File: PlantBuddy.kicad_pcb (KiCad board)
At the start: 4 copper layers, 44.3 x 29.2 mm, 47 parts, among them J1 USB_C_Receptacle_USB2.0, J101 JST, J4 External, SW1 SW_Push, U1 LTR-303ALS-01, U101 TPS2051B, U102 ESP32-S3-MINI-1-N8, U103 TPS2051B, U2 SHTC3, U4 BQ24072RGT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

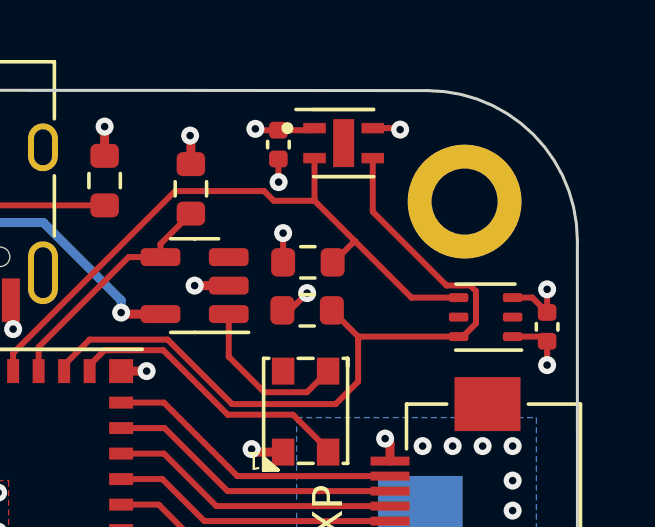
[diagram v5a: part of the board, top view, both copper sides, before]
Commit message: Added copper heatsink to temperature sensor.
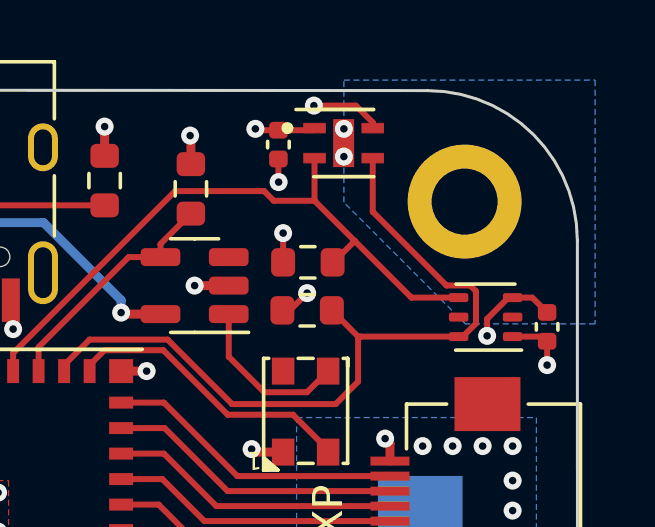
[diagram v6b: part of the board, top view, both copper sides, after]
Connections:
- H104 pad 1: GND -> unconnected-(U2-Pad5)
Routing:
- net GND: track 62.3 -> 64.7 mm
- net unconnected-(U2-Pad5): vias 0 -> 2
- added copper zone on B.Cu, net unconnected-(U2-Pad5)
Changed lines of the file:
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@@
     (fp_circle (center 0 0) (end 2.15 0) (layer "F.CrtYd") (width 0.05) (fill none))
     (pad "1" thru_hole circle locked (at 0 0) (size 3.8 3.8) (drill 2.2) (layers *.Cu *.Mask)
-      (net 6 "GND") (thermal_width 2))
+      (net 21 "unconnected-(U2-Pad5)") (thermal_width 2))
   )
   (footprint "Connector_Molex:Molex_PicoBlade_53261-0271_1x02-1MP_P1.25mm_Horizontal" (layer "F.Cu")
@@
   (segment (start 151.67533 131.381171) (end 150.51283 131.381171) (width 0.3) (layer "F.Cu") (net 6))
   (segment (start 126.01908 122.631171) (end 126.01908 121.731171) (width 0.2) (layer "F.Cu") (net 6))
+  (segment (start 152.74458 113.331171) (end 151.34408 113.331171) (width 0.2) (layer "F.Cu") (net 6))
   (segment (start 150.41908 133.681171) (end 150.36908 133.631171) (width 0.3) (layer "F.Cu") (net 6))
   (segment (start 147.29408 139.356027) (end 147.29408 138.456171) (width 0.2) (layer "F.Cu") (net 6))
+  (segment (start 153.30658 113.893171) (end 152.74458 113.331171) (width 0.2) (layer "F.Cu") (net 6))
   (segment (start 126.31908 127.256171) (end 126.29408 127.281171) (width 0.2) (layer "F.Cu") (net 6))
   (segment (start 125.57308 128.689671) (end 125.57308 127.967221) (width 0.2) (layer "F.Cu") (net 6))
@@
   (segment (start 141.24408 120.706171) (end 141.31908 120.781171) (width 0.3) (layer "F.Cu") (net 6))
   (segment (start 146.46908 136.461171) (end 146.46908 137.281171) (width 0.2) (layer "F.Cu") (net 6))
+  (segment (start 153.30658 114.081171) (end 153.30658 113.893171) (width 0.2) (layer "F.Cu") (net 6))
   (segment (start 150.51283 131.381171) (end 150.46283 131.431171) (width 0.3) (layer "F.Cu") (net 6))
   (segment (start 146.46908 134.511171) (end 146.84908 134.131171) (width 0.3) (layer "F.Cu") (net 6))
@@
   (segment (start 123.24408 122.756171) (end 123.26908 122.731171) (width 0.3) (layer "F.Cu") (net 6))
   (segment (start 148.04408 137.131171) (end 148.04408 138.056171) (width 0.2) (layer "F.Cu") (net 6))
+  (segment (start 157.96908 119.731171) (end 157.828804 119.731171) (width 0.2) (layer "F.Cu") (net 6))
   (segment (start 130.91908 133.431171) (end 130.91908 132.581171) (width 0.3) (layer "F.Cu") (net 6))
+  (segment (start 157.828804 119.731171) (end 157.11908 120.440895) (width 0.2) (layer "F.Cu") (net 6))
   (segment (start 153.881499 125.181171) (end 153.881499 124.59359) (width 0.3) (layer "F.Cu") (net 6))
   (segment (start 147.86283 130.776171) (end 147.08908 130.776171) (width 0.3) (layer "F.Cu") (net 6))
@@
   (segment (start 144.91908 135.131171) (end 144.91908 134.281171) (width 0.3) (layer "F.Cu") (net 6))
   (segment (start 130.91908 136.181171) (end 144.91908 136.181171) (width 0.3) (layer "F.Cu") (net 6))
-  (segment (start 154.16908 114.081171) (end 154.21908 114.131171) (width 0.2) (layer "F.Cu") (net 6))
+  (segment (start 157.11908 120.440895) (end 157.11908 121.006171) (width 0.2) (layer "F.Cu") (net 6))
   (segment (start 139.56908 130.831171) (end 139.56908 129.181171) (width 0.3) (layer "F.Cu") (net 6))
   (segment (start 127.59408 121.856171) (end 127.56908 121.831171) (width 0.2) (layer "F.Cu") (net 6))
@@
   (segment (start 125.56908 128.693671) (end 125.45658 128.693671) (width 0.3) (layer "F.Cu") (net 6))
   (segment (start 123.24408 128.906171) (end 123.51908 129.181171) (width 0.3) (layer "F.Cu") (net 6))
-  (segment (start 159.11908 120.226171) (end 159.11908 119.456171) (width 0.2) (layer "F.Cu") (net 6))
   (segment (start 126.06908 125.818671) (end 126.06908 125.134671) (width 0.2) (layer "F.Cu") (net 6))
   (segment (start 148.50658 119.331171) (end 147.36908 119.331171) (width 0.3) (layer "F.Cu") (net 6))
@@
   (segment (start 134.74408 119.816171) (end 134.74408 120.256171) (width 0.3) (layer "F.Cu") (net 6))
   (segment (start 123.14408 130.256171) (end 123.14408 130.956171) (width 0.3) (layer "F.Cu") (net 6))
-  (segment (start 153.30658 114.081171) (end 154.16908 114.081171) (width 0.2) (layer "F.Cu") (net 6))
   (segment (start 127.75658 117.331171) (end 128.99408 117.331171) (width 0.3) (layer "F.Cu") (net 6))
   (segment (start 125.44408 133.406171) (end 125.44408 134.456171) (width 0.3) (layer "F.Cu") (net 6))
@@
   (via (at 154.96908 124.681171) (size 0.6) (drill 0.25) (layers "F.Cu" "B.Cu") (free) (net 6))
   (via (at 135.06908 131.931171) (size 0.6) (drill 0.25) (layers "F.Cu" "B.Cu") (free) (net 6))
-  (via (at 159.11908 119.456171) (size 0.6) (drill 0.25) (layers "F.Cu" "B.Cu") (net 6))
   (via (at 135.06908 127.531171) (size 0.6) (drill 0.25) (layers "F.Cu" "B.Cu") (free) (net 6))
   (via (at 139.56908 126.231171) (size 0.6) (drill 0.25) (layers "F.Cu" "B.Cu") (free) (net 6))
@@
   (via (at 153.71908 124.431171) (size 0.6) (drill 0.25) (layers "F.Cu" "B.Cu") (net 6))
   (via (at 140.81908 129.181171) (size 0.6) (drill 0.25) (layers "F.Cu" "B.Cu") (free) (net 6))
-  (via (at 154.21908 114.131171) (size 0.6) (drill 0.25) (layers "F.Cu" "B.Cu") (net 6))
   (via (at 123.26908 122.731171) (size 0.6) (drill 0.25) (layers "F.Cu" "B.Cu") (net 6))
   (via (at 123.51908 129.181171) (size 0.6) (drill 0.25) (layers "F.Cu" "B.Cu") (net 6))
@@
   (via (at 136.21908 135.131171) (size 0.6) (drill 0.25) (layers "F.Cu" "B.Cu") (free) (net 6))
   (via (at 134.11908 120.881171) (size 0.6) (drill 0.25) (layers "F.Cu" "B.Cu") (net 6))
+  (via (at 151.34408 113.331171) (size 0.6) (drill 0.25) (layers "F.Cu" "B.Cu") (net 6))
   (via (at 137.91908 135.131171) (size 0.6) (drill 0.25) (layers "F.Cu" "B.Cu") (free) (net 6))
   (via (at 156.96908 124.681171) (size 0.6) (drill 0.25) (layers "F.Cu" "B.Cu") (free) (net 6))
@@
   (via (at 150.36908 133.631171) (size 0.6) (drill 0.25) (layers "F.Cu" "B.Cu") (net 6))
   (via (at 148.01908 138.081171) (size 0.6) (drill 0.25) (layers "F.Cu" "B.Cu") (net 6))
+  (via (at 157.11908 121.006171) (size 0.6) (drill 0.25) (layers "F.Cu" "B.Cu") (net 6))
   (via (at 137.91908 126.231171) (size 0.6) (drill 0.25) (layers "F.Cu" "B.Cu") (free) (net 6))
   (via (at 129.21908 121.831171) (size 0.6) (drill 0.25) (layers "F.Cu" "B.Cu") (net 6))
@@
   (segment (start 144.61908 131.731171) (end 144.06908 131.731171) (width 0.2) (layer "B.Cu") (net 19))
   (segment (start 132.01908 132.581171) (end 129.71908 132.581171) (width 0.2) (layer "B.Cu") (net 19))
+  (via (at 152.34408 115.031171) (size 0.6) (drill 0.25) (layers "F.Cu" "B.Cu") (net 21))
+  (via (at 152.34408 114.106171) (size 0.6) (drill 0.25) (layers "F.Cu" "B.Cu") (net 21))
   (segment (start 137.24408 119.816171) (end 137.24408 118.862571) (width 0.2286) (layer "F.Cu") (net 22))
   (segment (start 138.01238 118.824471) (end 138.24408 119.056171) (width 0.2286) (layer "F.Cu") (net 22))
@@
     )
   )
+  (zone (net 21) (net_name "unconnected-(U2-Pad5)") (layer "B.Cu") (hatch edge 0.508)
+    (connect_pads (clearance 0))
+    (min_thickness 0.254) (filled_areas_thickness no)
+    (fill yes (thermal_gap 0.508) (thermal_bridge_width 0.508))
+    (polygon
+      (pts
+        (xy 160.71908 120.606171)
+        (xy 156.39408 120.606171)
+        (xy 152.34408 116.556171)
+        (xy 152.34408 112.481171)
+        (xy 160.71908 112.481171)
+      )
+    )
+  )
   (zone (net 6) (net_name "GND") (layer "B.Cu") (hatch edge 0.508)
     (connect_pads (clearance 0))
@@
       )
     )
+  )
+  (zone (net 0) (net_name "") (layer "B.Mask") (hatch edge 0.508)
+    (connect_pads (clearance 0))
+    (min_thickness 0.254) (filled_areas_thickness no)
+    (fill yes (thermal_gap 0.508) (thermal_bridge_width 0.508))
+    (polygon
+      (pts
+        (xy 160.71908 120.606171)
+        (xy 156.39408 120.606171)
+        (xy 152.34408 116.556171)
+        (xy 152.34408 112.481171)
+        (xy 160.71908 112.481171)
+      )
+    )

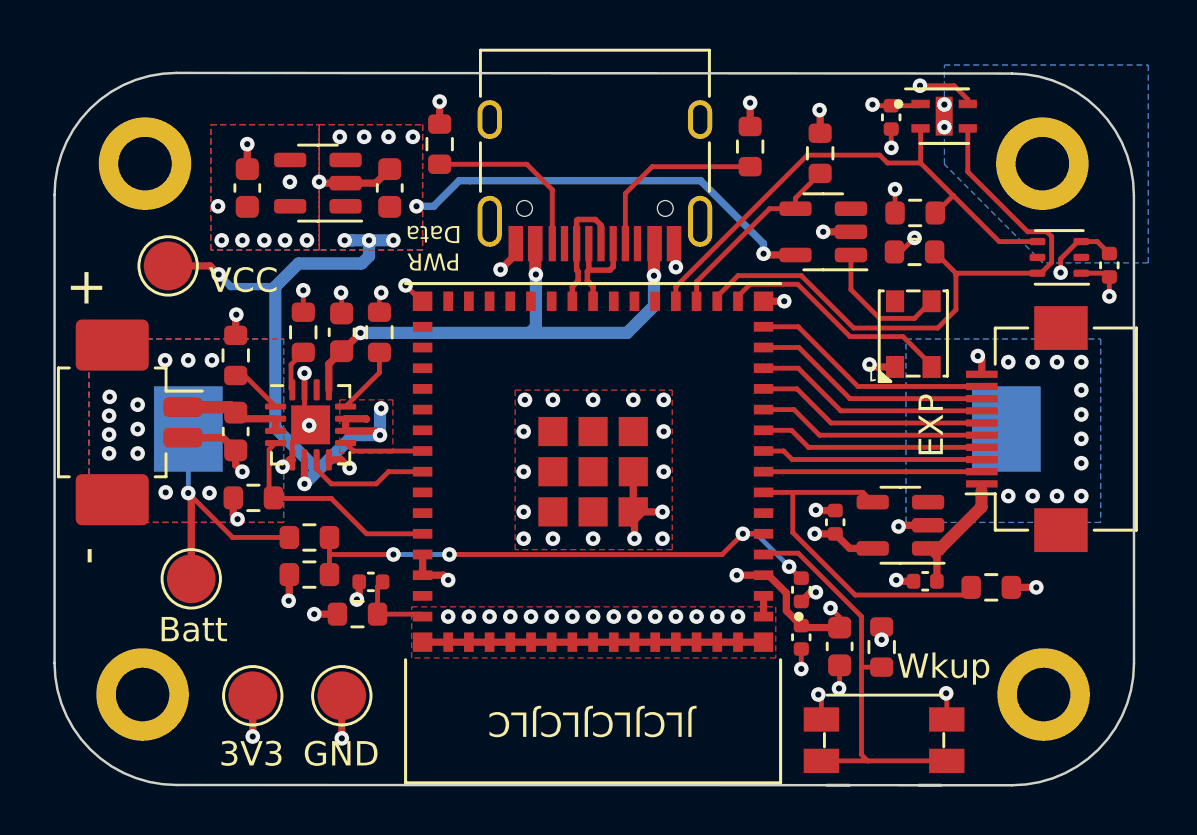
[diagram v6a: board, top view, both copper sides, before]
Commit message: Multitude of changes. Hopefully design freeze.
- Switched JST connector to a bigger 2mm pitch one.
- Added battery protection circuit for coin cell.
- Created cutout in PCB for battery cable.
- Added heatsink for SHTC3.
- Added plated mounting holes for looks and power dissipation.
- Changed pin layout to facilitate wake-up via USB-C plug-in detection.
- Added ARTech logo.
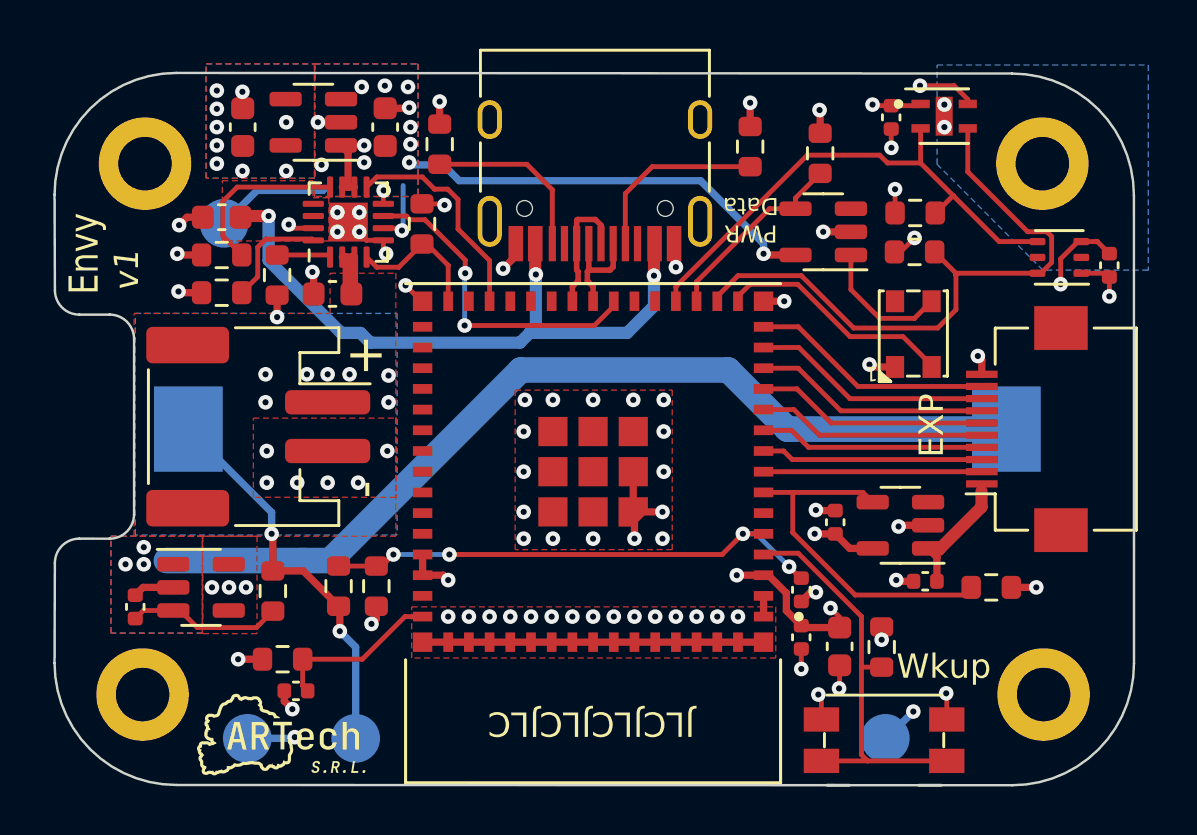
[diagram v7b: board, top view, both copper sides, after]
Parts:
- added C104: 100nF, Capacitor_SMD:C_0402_1005Metric, F.Cu at (119.1, 134.7)
- added G***: LOGO, LOGO, F.Cu at (125.2, 139.9)
- added R103: 100R, Resistor_SMD:R_0603_1608Metric, F.Cu at (124.8, 134.1)
- added U104: XB5350A, Package_TO_SOT_SMD:SOT-23-5, F.Cu at (121.8, 133.9)
- J101: footprint Connector_Molex:Molex_PicoBlade_53261-0271_1x02-1MP_P1.25mm_Horizontal -> Connector_JST:JST_PH_S2B-PH-SM4-TB_1x02-1MP_P2.00mm_Horizontal
- R6: value 15k -> 9.1k
- R8, R9: value 15k -> 10k
- TP1, TP101, TP102, TP2: moved to B.Cu
- moved TP1 26.0 mm to (149.9, 140.1), turned to 180 degrees
- moved R9 13.2 mm to (130.9, 119.0), turned to -90 degrees
- moved TP102 9.41 mm to (128.2, 140.1), turned to 180 degrees
- moved U4 8.47 mm to (127.9, 118.9), turned to 90 degrees
- moved R5 7.21 mm to (122.7, 120.3), turned to 0 degrees
- moved C6 6.91 mm to (127.2, 121.9), turned to 0 degrees
- moved C5 6.83 mm to (122.7, 118.7), turned to 180 degrees
- moved J101 5.50 mm to (124.2, 127.3)
- moved C3 5.43 mm to (125.7, 138.2)
- moved TP2 4.26 mm to (123.7, 140.1), turned to 180 degrees
- moved R6 3.72 mm to (122.7, 121.8), turned to 0 degrees
- moved R10 3.71 mm to (124.9, 121.1), turned to -90 degrees
- moved R8 3.59 mm to (125.2, 136.9)
- moved TP101 2.89 mm to (122.8, 119.0), turned to 180 degrees
- moved R14 2.79 mm to (129.0, 133.9), turned to -90 degrees
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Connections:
- BT1 pad 2: GND -> /Bat_n
- H104 pad 1: unconnected-(U2-Pad5) -> /Heat
- U102 pad 22: unconnected-(U102-Pad22) -> /~PGOOD
- U102 pad 28: unconnected-(U102-Pad28) -> /~CHG
- U102 pad 30: unconnected-(U102-Pad30) -> /charge_disable
- U102 pad 37: /~CHG -> unconnected-(U102-Pad37)
- U102 pad 38: /~PGOOD -> unconnected-(U102-Pad38)
- U102 pad 41: /charge_disable -> unconnected-(U102-Pad41)
- U2 pad 5: unconnected-(U2-Pad5) -> /Heat
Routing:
- net /Bat_n: track 0.00 -> 40.7 mm, vias 0 -> 3
- net VCC: track 46.4 -> 27.4 mm, vias 13 -> 11
- net /~PGOOD: track 5.19 -> 13.5 mm, vias 0 -> 2
- net Net-(C104-Pad1): track 0.00 -> 6.36 mm
- net +BATT: track 15.6 -> 21.5 mm, vias 13 -> 9
- net /~CHG: track 3.30 -> 9.03 mm
- net VBUS: track 21.8 -> 27.2 mm
- net Net-(R5-Pad2): track 2.80 -> 7.16 mm
- net GND: track 64.7 -> 60.4 mm, vias 79 -> 80
- net /~{tRST}: track 3.30 -> 7.03 mm
- net /charge_disable: track 9.17 -> 5.76 mm
- net Net-(R6-Pad2): track 1.77 -> 4.58 mm
- net /batsense: track 22.9 -> 21.2 mm
- net +3V3: vias 19 -> 20
- net unconnected-(U2-Pad5): vias 2 -> 0
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- added copper zone on B.Cu, net /Bat_n
- added copper zone on F.Cu, net /Bat_n
- added copper zone on B.Cu, net /Heat
- added copper zone on F.Cu, net VBUS
- removed copper zone on B.Cu, net GND
- removed copper zone on B.Cu, net unconnected-(U2-Pad5)
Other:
- outline, holes or cut-outs redrawn
- board text added: "Envy"
- board text added: "v1"

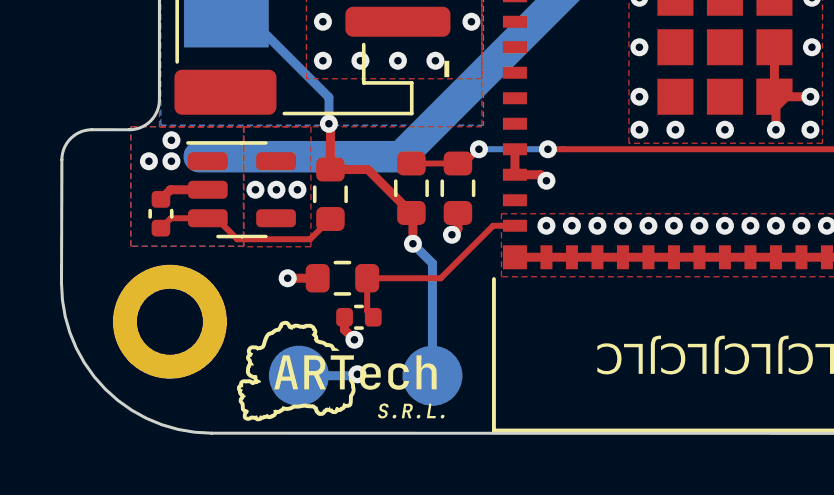
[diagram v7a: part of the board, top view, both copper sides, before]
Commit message: Added Voltage Supervisor circuit.
LMS33460 is used as a voltage supervisor circuit meant to protect the
ESP32, as well as the battery, if a low-voltage condition is detected.
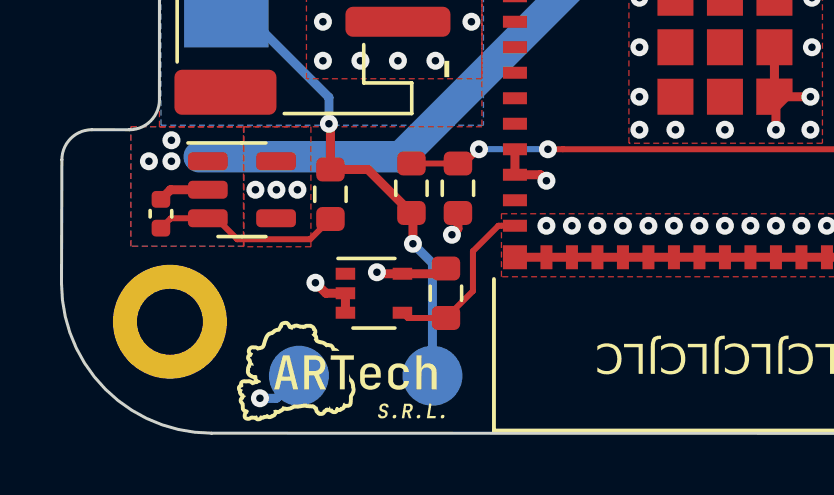
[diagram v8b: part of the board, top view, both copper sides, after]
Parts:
- removed C3: 100nF, Capacitor_SMD:C_0402_1005Metric
- removed R8: 10k, Resistor_SMD:R_0603_1608Metric
- added R104: 470k, Resistor_SMD:R_0603_1608Metric, F.Cu at (128.6, 137.4)
- added U105: LMS33460MG, Package_TO_SOT_SMD:SOT-353_SC-70-5, F.Cu at (126.2, 137.4)
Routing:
- net +3V3: track 20.3 -> 21.7 mm
- net /~{tRST}: track 7.03 -> 5.87 mm
- net GND: track 60.4 -> 61.0 mm
